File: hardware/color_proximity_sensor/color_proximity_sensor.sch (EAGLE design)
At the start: 54 parts, among them IC1 TCS37725FN, IC2 APDS-9800-021, IC3 NCV78M05BDTRKG, IC4 LM25011MY, T1 mmbt2222, T2 mmbt2222, T3 mmbt2222

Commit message: microcontroler added
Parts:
- added C13, C14, C15, C16, C17: 100nF 50V, robotter_capacitor:100NF-F
- added C18, C19: 15pF_0603_100V, robotter_capacitor:15PF-F
- added IC5: ATXMEGA64DA-AU, robotter_ic:ATXMEGA64D4-AU
- added L2: 220 ohms, robotter_inductor:FERRITE_220OHMS
- added Q1: 16 MHz, robotter_ic:CRYSTAL_16MHZ_HC49UP
- added R19, R20, R21, R23, R25: 10K-F, robotter_resistor:10K-F
- added SV1: (no value), robotter_connector:PDI_ATMELL
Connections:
- net VBAT renamed +24V
- new net COLOR_DATA0_3V3: IC5.PB1/ADCA9
- new net COLOR_DATA1_3V3: IC5.PB2/ADCA10
- new net COLOR_DATA2_3V3: IC5.PB3/ADCA11
- new net COLOR_VALID_OUT_3V3: IC5.PB0/ADCA8/AREF
- new net N$17: C13.1, IC5.AVCC@0, L2.1
- new net N$19: C18.1, IC5.PR1/XTAL1, Q1.1
- new net N$20: C19.1, IC5.PR0/XTAL2, Q1.2
- new net PDI_CLK_3V3: IC5./RESET, R19.1, SV1.CLK
- new net PDI_DATA_3V3: IC5.PDI, SV1.DATA
- new net RX_3V3: IC5.PC2/OC0C/RXD0, R23.2
- new net TX_3V3: IC5.PC3/OC0D/TXD0, R21.2
- net +3V3: now also C14.1, C15.1, C16.1, C17.1, IC5.VCC@0, IC5.VCC@1, IC5.VCC@2, L2.2, R19.2, R21.1, R23.1, SV1.VCC
- net APDS_AMBIENT_0-300MV: now also IC5.PA5/ADCA5
- net APDS_ENABLE_3V3: now also IC5.PC5/OC1B/MOSI
- net APDS_LED_PWM_3V3: now also IC5.PC4/OC1A/\S\S
- net APDS_OUTPUT_3V3: now also IC5.PC6/MISO
- net APDS_PROXIMITY_ANA_0-0.65V: now also IC5.PA4/ADCA4
- net BATTERY_MONITOR_0-1V: now also IC5.PA0/ADCA0/AREF
- net GND: now also C13.2, C14.2, C15.2, C16.2, C17.2, C18.2, C19.2, IC5.GND@0, IC5.GND@1, IC5.GND@2, IC5.GND@3, SV1.GND
- net INT_TCS37725_3V3: now also IC5.PC7/SCK
- net LED_BLUE_CMD_3V3: now also IC5.SDA/OC0A/PE0
- net LED_GREEN_CMD_3V3: now also IC5.OC0C/PE2
- net LED_RED_CMD_3V3: now also IC5.SCL/OC0B/PE1
- net SCL_3V3: now also IC5.PC1/OC0B/XCK0/SCL, R20.1
- net SDA_3V3: now also IC5.PC0/OC0A/SDA, R25.1
- net VCC: now also R20.2, R25.2
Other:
- note added: "color_valid_3v3, color_data*_3v3 are outputs of this board. color_valid_3v3 is high when data on color_data*_3v3 is valid, else 0 when data state is updated"
- note added: "manque alim"
- note added: "manque connecteur meca"

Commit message: add board, routing in process
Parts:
- removed C21, C34: 10µF 25V, robotter_capacitor:10UF-C_25V
- removed IC3: NCV78M05BDTRKG, linear:NCV78M05BDTRKG
- removed R11, R12, R15: 10K-F, robotter_resistor:10K-F
- removed R59: 100_1W-1W, robotter_resistor:100_1W-1W
- removed SV1: (no value), robotter_connector:PDI_ATMELL
- removed T2, T3: mmbt2222, robotter_ic:MMBT2222ALT1-NPN-SOT23-BEC
- added COM: MICROMATCH-8_SMD, robotter_connector:MICROMATCH-8_SMD
- added H1, H3: MOUNT-PAD-ROUND, robotter_others:MOUNT-PAD-ROUND
- added J1: PDI_ATMEL_WIDTH, robotter_connector:PDI_ATMEL_WIDTH
- added T4: BC847CDXV6T1G, robotter_ic:BC847CDXV6T
- C2: value 330µF 35V -> 220µF 35V; device robotter_capacitor:330UF -> robotter_capacitor:220UFF_35V
- T1: value mmbt2222 -> BC847CDXV6T1G; device robotter_ic:MMBT2222ALT1-NPN-SOT23-BEC -> robotter_ic:BC847CDXV6T
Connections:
- net VCC renamed TCS_VCC
- removed net +5V: C34.1, IC3.VO
- removed net N$41: C21.1, IC3.VI, R59.2
- net +24V: now also COM-8.S, R16.2, R17.2, R18.2; no longer LED3_B.A, LED3_G.A, LED3_R.A, R59.1
- net +3V3: now also J1.VCC; no longer SV1.VCC
- net APDS_ENABLE_3V3: now also IC5.\S\S/PD4; no longer IC5.PC5/OC1B/MOSI
- net APDS_LED_PWM_3V3: now also IC5.TXD0/OC0D/PD3; no longer IC5.PC4/OC1A/\S\S
- net APDS_OUTPUT_3V3: now also IC5.MOSI/PD5; no longer IC5.PC6/MISO
- net COLOR_DATA0_3V3: now also COM-3.S
- net COLOR_DATA1_3V3: now also COM-2.S
- net COLOR_DATA2_3V3: now also COM-1.S
- net COLOR_VALID_OUT_3V3: now also COM-4.S
- net GND: now also COM-5.S, H1.MOUNT, H3.MOUNT, J1.GND, T1-Q1.B, T1-Q1.C, T1-Q1.E, T1-Q2.E, T4-Q1.E, T4-Q2.E; no longer C21.2, C34.2, IC3.GND, R11.1, R12.1, R15.1, SV1.GND, T1.E, T2.E, T3.E
- net INT_TCS37725_3V3: now also IC5.SCK/PD7; no longer IC5.PC7/SCK
- net LED_BLUE_CMD_3V3: now also IC5.PC0/OC0A/SDA; no longer IC5.SDA/OC0A/PE0, R15.2
- net LED_GREEN_CMD_3V3: now also IC5.PC4/OC1A/\S\S; no longer IC5.OC0C/PE2, R12.2
- net LED_RED_CMD_3V3: now also IC5.PC1/OC0B/XCK0/SCL; no longer IC5.SCL/OC0B/PE1, R11.2
- net N$1: now also T4-Q1.B; no longer T1.B
- net N$11: now also LED3_G.A; no longer T2.C
- net N$12: now also LED3_B.A, R16.1; no longer R18.1, T3.C
- net N$3: now also T4-Q2.B; no longer T2.B
- net N$5: now also T1-Q2.B; no longer T3.B
- net N$6: now also LED3_R.A, R18.1; no longer R16.1, T1.C
- net N$7: now also LED2_G.C, T4-Q2.C; no longer LED2_B.C, R16.2
- net N$8: now also LED2_R.C, T1-Q2.C; no longer LED2_G.C, R17.2
- net N$9: now also LED2_B.C, T4-Q1.C; no longer LED2_R.C, R18.2
- net PDI_CLK_3V3: now also J1.CLK; no longer SV1.CLK
- net PDI_DATA_3V3: now also J1.DATA; no longer SV1.DATA
- net RX_3V3: now also COM-6.S
- net SCL_3V3: now also IC5.SCL/OC0B/PE1; no longer IC5.PC1/OC0B/XCK0/SCL
- net SDA_3V3: now also IC5.SDA/OC0A/PE0; no longer IC5.PC0/OC0A/SDA
- net TX_3V3: now also COM-7.S
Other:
- moved on the sheet: C10, C11, C12, C2, C22, C30, C31, C32, C33, D8, IC4, L1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

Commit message: board routed
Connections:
- net +24V: now also COM-7.S; no longer COM-8.S
- net APDS_AMBIENT_0-300MV: now also IC5.PA0/ADCA0/AREF; no longer IC5.PA5/ADCA5
- net APDS_PROXIMITY_ANA_0-0.65V: now also IC5.PA1/ADCA1; no longer IC5.PA4/ADCA4
- net BATTERY_MONITOR_0-1V: now also IC5.PA5/ADCA5; no longer IC5.PA0/ADCA0/AREF
- net COLOR_DATA0_3V3: now also COM-6.S; no longer COM-3.S
- net COLOR_DATA1_3V3: now also COM-5.S; no longer COM-2.S
- net COLOR_DATA2_3V3: now also COM-4.S; no longer COM-1.S
- net COLOR_VALID_OUT_3V3: now also COM-8.S; no longer COM-4.S
- net GND: now also COM-1.S; no longer COM-5.S
- net LED_GREEN_CMD_3V3: now also IC5.PC1/OC0B/XCK0/SCL; no longer IC5.PC4/OC1A/\S\S
- net LED_RED_CMD_3V3: now also IC5.PC4/OC1A/\S\S; no longer IC5.PC1/OC0B/XCK0/SCL
- net RX_3V3: now also COM-3.S; no longer COM-6.S
- net TX_3V3: now also COM-2.S; no longer COM-7.S
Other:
- moved on the sheet: COM-1, COM-2, COM-3, COM-4, COM-5, COM-6, COM-7, COM-8
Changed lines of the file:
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@@
 <instance part="C19" gate="G$1" x="157.48" y="256.54"/>
 <instance part="Q1" gate="G$1" x="144.78" y="264.16"/>
-<instance part="GND14" gate="1" x="335.28" y="45.72"/>
+<instance part="GND14" gate="1" x="327.66" y="43.18"/>
 <instance part="P+1" gate="1" x="55.88" y="157.48"/>
 <instance part="P+2" gate="1" x="309.88" y="144.78"/>
@@
 <instance part="H3" gate="G$1" x="454.66" y="58.42" rot="R90"/>
 <instance part="GND15" gate="1" x="444.5" y="53.34"/>
-<instance part="COM" gate="-1" x="284.48" y="22.86"/>
-<instance part="COM" gate="-2" x="284.48" y="27.94"/>
-<instance part="COM" gate="-3" x="284.48" y="33.02"/>
-<instance part="COM" gate="-4" x="284.48" y="38.1"/>
-<instance part="COM" gate="-5" x="284.48" y="48.26"/>
-<instance part="COM" gate="-6" x="284.48" y="53.34"/>
-<instance part="COM" gate="-7" x="284.48" y="58.42"/>
-<instance part="COM" gate="-8" x="284.48" y="63.5"/>
+<instance part="COM" gate="-1" x="284.48" y="43.18"/>
+<instance part="COM" gate="-2" x="284.48" y="58.42"/>
+<instance part="COM" gate="-3" x="284.48" y="53.34"/>
+<instance part="COM" gate="-4" x="284.48" y="22.86"/>
+<instance part="COM" gate="-5" x="284.48" y="27.94"/>
+<instance part="COM" gate="-6" x="284.48" y="33.02"/>
+<instance part="COM" gate="-7" x="284.48" y="63.5"/>
+<instance part="COM" gate="-8" x="284.48" y="38.1"/>
 <instance part="J1" gate="G$1" x="127" y="198.12"/>
 <instance part="T4" gate="-Q2" x="106.68" y="58.42"/>
@@
 </segment>
 <segment>
-<pinref part="GND14" gate="1" pin="GND"/>
-<wire x1="289.56" y1="48.26" x2="335.28" y2="48.26" width="0.1524" layer="91"/>
-<pinref part="COM" gate="-5" pin="S"/>
-</segment>
-<segment>
 <wire x1="434.34" y1="55.88" x2="444.5" y2="55.88" width="0.1524" layer="91"/>
 <pinref part="H3" gate="G$1" pin="MOUNT"/>
@@
 <pinref part="GND16" gate="1" pin="GND"/>
 <junction x="167.64" y="38.1"/>
+</segment>
+<segment>
+<pinref part="COM" gate="-1" pin="S"/>
+<pinref part="GND14" gate="1" pin="GND"/>
+<wire x1="327.66" y1="45.72" x2="292.1" y2="45.72" width="0.1524" layer="91"/>
+<wire x1="292.1" y1="45.72" x2="292.1" y2="43.18" width="0.1524" layer="91"/>
+<wire x1="292.1" y1="43.18" x2="289.56" y2="43.18" width="0.1524" layer="91"/>
 </segment>
 </net>
@@
 </segment>
 <segment>
-<pinref part="IC5" gate="G$1" pin="PA0/ADCA0/AREF"/>
-<wire x1="68.58" y1="314.96" x2="30.48" y2="314.96" width="0.1524" layer="91"/>
-<label x="30.48" y="314.96" size="1.778" layer="95"/>
+<pinref part="IC5" gate="G$1" pin="PA5/ADCA5"/>
+<wire x1="68.58" y1="302.26" x2="27.94" y2="302.26" width="0.1524" layer="91"/>
+<label x="27.94" y="302.26" size="1.778" layer="95"/>
 </segment>
 </net>
@@
 </segment>
 <segment>
-<pinref part="IC5" gate="G$1" pin="PA4/ADCA4"/>
-<wire x1="68.58" y1="304.8" x2="30.48" y2="304.8" width="0.1524" layer="91"/>
-<label x="30.48" y="304.8" size="1.778" layer="95"/>
+<pinref part="IC5" gate="G$1" pin="PA1/ADCA1"/>
+<wire x1="68.58" y1="312.42" x2="25.4" y2="312.42" width="0.1524" layer="91"/>
+<label x="25.4" y="312.42" size="1.778" layer="95"/>
 </segment>
 </net>
@@
 </segment>
 <segment>
-<pinref part="IC5" gate="G$1" pin="PA5/ADCA5"/>
-<wire x1="68.58" y1="302.26" x2="30.48" y2="302.26" width="0.1524" layer="91"/>
-<label x="30.48" y="302.26" size="1.778" layer="95"/>
+<pinref part="IC5" gate="G$1" pin="PA0/ADCA0/AREF"/>
+<wire x1="68.58" y1="314.96" x2="25.4" y2="314.96" width="0.1524" layer="91"/>
+<label x="25.4" y="314.96" size="1.778" layer="95"/>
 </segment>
 </net>
@@
 </segment>
 <segment>
+<pinref part="IC5" gate="G$1" pin="PC4/OC1A/\S\S"/>
+<wire x1="68.58" y1="264.16" x2="38.1" y2="264.16" width="0.1524" layer="91"/>
+<label x="38.1" y="264.16" size="1.778" layer="95"/>
+</segment>
+</net>
+<net name="LED_GREEN_CMD_3V3" class="0">
+<segment>
+<pinref part="R9" gate="G$1" pin="1"/>
+<wire x1="91.44" y1="58.42" x2="20.32" y2="58.42" width="0.1524" layer="91"/>
+<label x="20.32" y="58.42" size="1.778" layer="95"/>
+</segment>
+<segment>
 <pinref part="IC5" gate="G$1" pin="PC1/OC0B/XCK0/SCL"/>
 <wire x1="68.58" y1="271.78" x2="38.1" y2="271.78" width="0.1524" layer="91"/>
 <label x="38.1" y="271.78" size="1.778" layer="95"/>
-</segment>
-</net>
-<net name="LED_GREEN_CMD_3V3" class="0">
-<segment>
-<pinref part="R9" gate="G$1" pin="1"/>
-<wire x1="91.44" y1="58.42" x2="20.32" y2="58.42" width="0.1524" layer="91"/>
-<label x="20.32" y="58.42" size="1.778" layer="95"/>
-</segment>
-<segment>
-<pinref part="IC5" gate="G$1" pin="PC4/OC1A/\S\S"/>
-<wire x1="68.58" y1="264.16" x2="38.1" y2="264.16" width="0.1524" layer="91"/>
-<label x="38.1" y="264.16" size="1.778" layer="95"/>
 </segment>
 </net>
@@
 <wire x1="289.56" y1="58.42" x2="327.66" y2="58.42" width="0.1524" layer="91"/>
 <label x="294.64" y="58.42" size="1.778" layer="95"/>
-<pinref part="COM" gate="-7" pin="S"/>
+<pinref part="COM" gate="-2" pin="S"/>
 </segment>
 <segment>
@@
 <segment>
 <label x="294.64" y="53.34" size="1.778" layer="95"/>
-<pinref part="COM" gate="-6" pin="S"/>
 <wire x1="289.56" y1="53.34" x2="327.66" y2="53.34" width="0.1524" layer="91"/>
+<pinref part="COM" gate="-3" pin="S"/>
 </segment>
 <segment>
@@
 <wire x1="335.28" y1="63.5" x2="289.56" y2="63.5" width="0.1524" layer="91"/>
 <pinref part="P+3" gate="1" pin="+24V"/>
-<pinref part="COM" gate="-8" pin="S"/>
+<pinref part="COM" gate="-7" pin="S"/>
 </segment>
 </net>
@@
 <wire x1="335.28" y1="38.1" x2="289.56" y2="38.1" width="0.1524" layer="91"/>
 <label x="294.64" y="38.1" size="1.778" layer="95"/>
-<pinref part="COM" gate="-4" pin="S"/>
+<pinref part="COM" gate="-8" pin="S"/>
 </segment>
 <segment>
@@
 <wire x1="289.56" y1="33.02" x2="335.28" y2="33.02" width="0.1524" layer="91"/>
 <label x="294.64" y="33.02" size="1.778" layer="95"/>
-<pinref part="COM" gate="-3" pin="S"/>
+<pinref part="COM" gate="-6" pin="S"/>
 </segment>
 <segment>
@@
 <wire x1="289.56" y1="27.94" x2="335.28" y2="27.94" width="0.1524" layer="91"/>
 <label x="294.64" y="27.94" size="1.778" layer="95"/>
-<pinref part="COM" gate="-2" pin="S"/>
+<pinref part="COM" gate="-5" pin="S"/>
 </segment>
 <segment>
@@
 <wire x1="289.56" y1="22.86" x2="335.28" y2="22.86" width="0.1524" layer="91"/>
 <label x="294.64" y="22.86" size="1.778" layer="95"/>
-<pinref part="COM" gate="-1" pin="S"/>
-</segment>
-</net>
+<pinref part="COM" gate="-4" pin="S"/>
+</segment>
+</net>

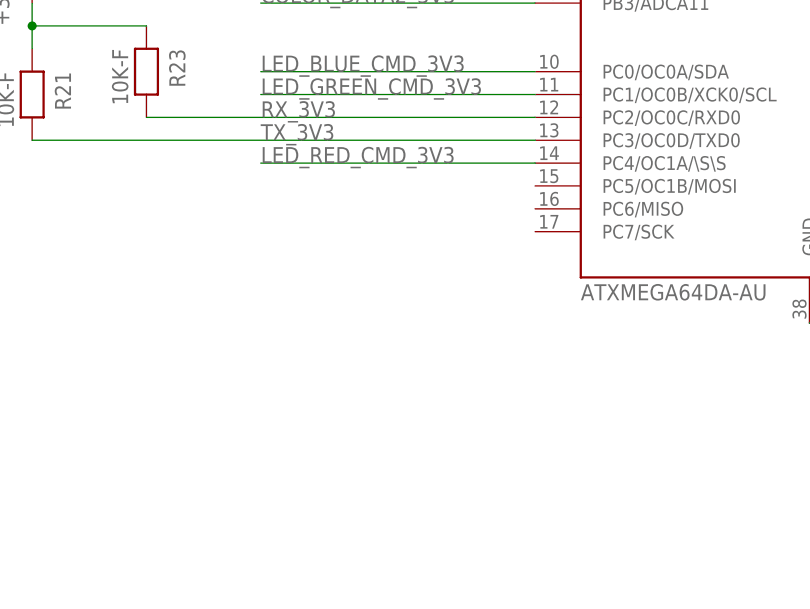
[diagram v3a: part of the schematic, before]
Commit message: silkscreen done
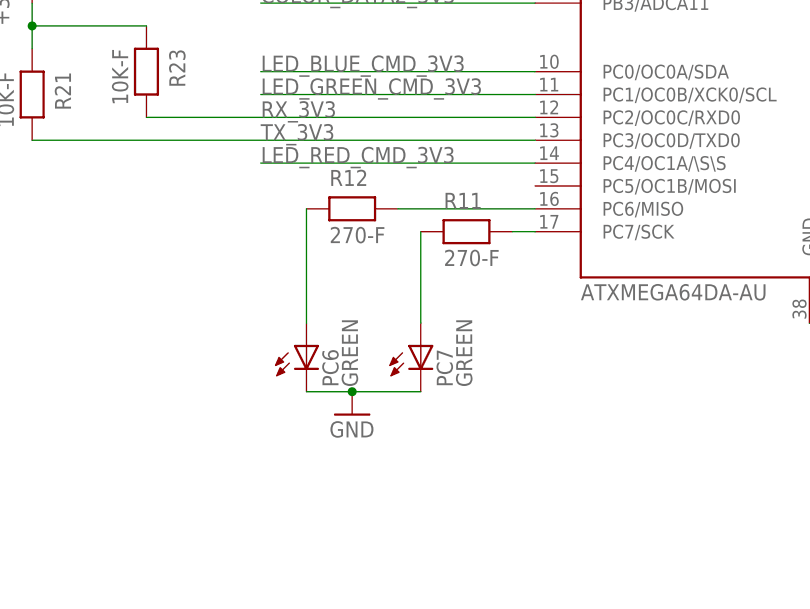
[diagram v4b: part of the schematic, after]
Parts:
- added PC6, PC7: GREEN, robotter_diode:LED_G
- added R11, R12: 270-F, robotter_resistor:270-F
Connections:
- new net N$13: IC5.PC7/SCK, R11.2
- new net N$16: IC5.PC6/MISO, R12.2
- new net N$21: PC7.A, R11.1
- new net N$22: PC6.A, R12.1
- net GND: now also PC6.C, PC7.C
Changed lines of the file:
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@@
 <part name="T1" library="robotter_ic" deviceset="BC847CDXV6T" device="" value="BC847CDXV6T1G"/>
 <part name="GND16" library="supply1" deviceset="GND" device=""/>
+<part name="PC6" library="robotter_diode" deviceset="LED_" device="G" value="GREEN"/>
+<part name="PC7" library="robotter_diode" deviceset="LED_" device="G" value="GREEN"/>
+<part name="R11" library="robotter_resistor" deviceset="270" device="-F"/>
+<part name="R12" library="robotter_resistor" deviceset="270" device="-F"/>
+<part name="GND17" library="supply1" deviceset="GND" device=""/>
 </parts>
 <sheets>
@@
 <instance part="T1" gate="-Q1" x="167.64" y="43.18"/>
 <instance part="GND16" gate="1" x="167.64" y="35.56"/>
+<instance part="PC6" gate="G$1" x="43.18" y="243.84"/>
+<instance part="PC7" gate="G$1" x="55.88" y="243.84"/>
+<instance part="R11" gate="G$1" x="60.96" y="256.54"/>
+<instance part="R12" gate="G$1" x="48.26" y="259.08"/>
+<instance part="GND17" gate="1" x="48.26" y="236.22"/>
 </instances>
 <busses>
@@
 <wire x1="292.1" y1="45.72" x2="292.1" y2="43.18" width="0.1524" layer="91"/>
 <wire x1="292.1" y1="43.18" x2="289.56" y2="43.18" width="0.1524" layer="91"/>
+</segment>
+<segment>
+<pinref part="PC6" gate="G$1" pin="C"/>
+<pinref part="PC7" gate="G$1" pin="C"/>
+<wire x1="43.18" y1="238.76" x2="48.26" y2="238.76" width="0.1524" layer="91"/>
+<pinref part="GND17" gate="1" pin="GND"/>
+<wire x1="48.26" y1="238.76" x2="55.88" y2="238.76" width="0.1524" layer="91"/>
+<junction x="48.26" y="238.76"/>
 </segment>
 </net>
@@
 </segment>
 </net>
+<net name="N$13" class="0">
+<segment>
+<pinref part="IC5" gate="G$1" pin="PC7/SCK"/>
+<pinref part="R11" gate="G$1" pin="2"/>
+<wire x1="66.04" y1="256.54" x2="68.58" y2="256.54" width="0.1524" layer="91"/>
+</segment>
+</net>
+<net name="N$16" class="0">
+<segment>
+<pinref part="IC5" gate="G$1" pin="PC6/MISO"/>
+<pinref part="R12" gate="G$1" pin="2"/>
+<wire x1="53.34" y1="259.08" x2="68.58" y2="259.08" width="0.1524" layer="91"/>
+</segment>
+</net>
+<net name="N$21" class="0">
+<segment>
+<pinref part="PC7" gate="G$1" pin="A"/>
+<pinref part="R11" gate="G$1" pin="1"/>
+<wire x1="55.88" y1="246.38" x2="55.88" y2="256.54" width="0.1524" layer="91"/>
+</segment>
+</net>
+<net name="N$22" class="0">
+<segment>
+<pinref part="R12" gate="G$1" pin="1"/>
+<pinref part="PC6" gate="G$1" pin="A"/>
+<wire x1="43.18" y1="259.08" x2="43.18" y2="246.38" width="0.1524" layer="91"/>
+</segment>
+</net>
